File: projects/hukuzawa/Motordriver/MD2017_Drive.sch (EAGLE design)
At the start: 3 parts

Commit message: ドライバ駆動部回路図製作経過
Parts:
- added U$4: BUK116-50L, BUK116-50L:BUK116-50L
- added U$5, U$6: RELAY(L), relay:RELAY(L)
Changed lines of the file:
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@@
 <part name="U$2" library="FH105" deviceset="8PIN" device=""/>
 <part name="U$3" library="FH105" deviceset="8PIN" device=""/>
+<part name="U$4" library="BUK116-50L" deviceset="BUK116-50L" device=""/>
+<part name="U$5" library="relay" deviceset="RELAY(L)" device=""/>
+<part name="U$6" library="relay" deviceset="RELAY(L)" device=""/>
 </parts>
 <sheets>
@@
 <instance part="U$3" gate="-7" x="83.82" y="-25.4"/>
 <instance part="U$3" gate="-1" x="83.82" y="5.08"/>
+<instance part="U$4" gate="G$1" x="-22.86" y="35.56"/>
+<instance part="U$5" gate="R1" x="-68.58" y="5.08" rot="R180"/>
+<instance part="U$5" gate="1" x="-48.26" y="10.16" rot="R180"/>
+<instance part="U$5" gate="R2" x="-68.58" y="25.4" rot="R180"/>
+<instance part="U$6" gate="R1" x="-68.58" y="-35.56" rot="R180"/>
+<instance part="U$6" gate="1" x="-48.26" y="-30.48" rot="R180"/>
+<instance part="U$6" gate="R2" x="-68.58" y="-17.78" rot="R180"/>
 </instances>
 <busses>

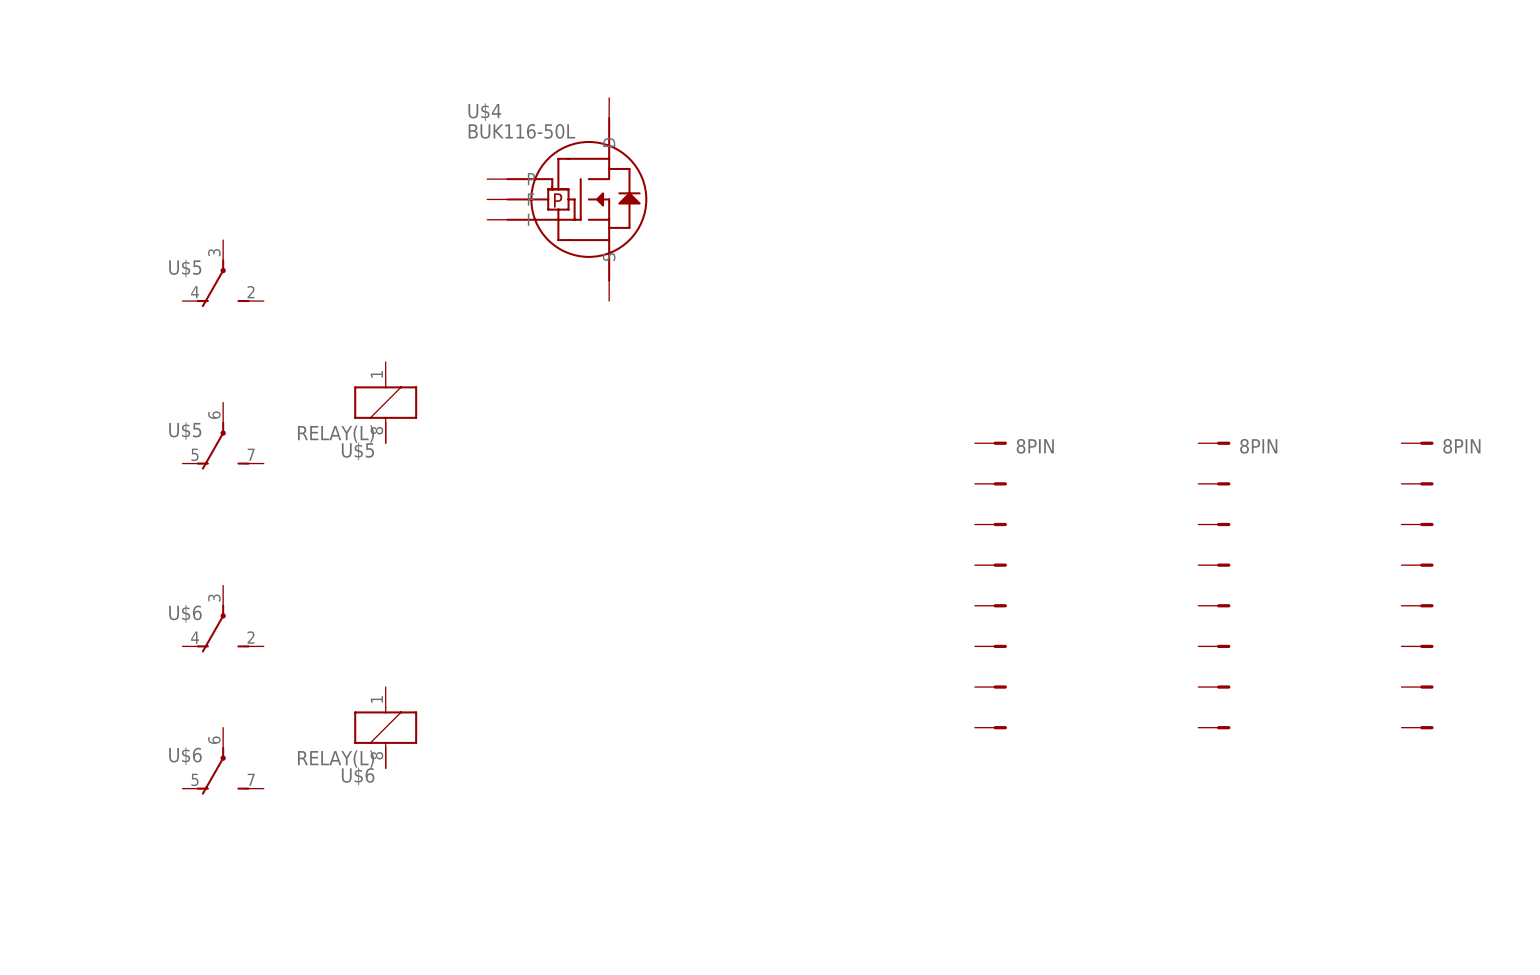
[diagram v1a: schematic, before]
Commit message: モータードライバ駆動部回路図製作途中
フォトカプラ追加、配線一部完了
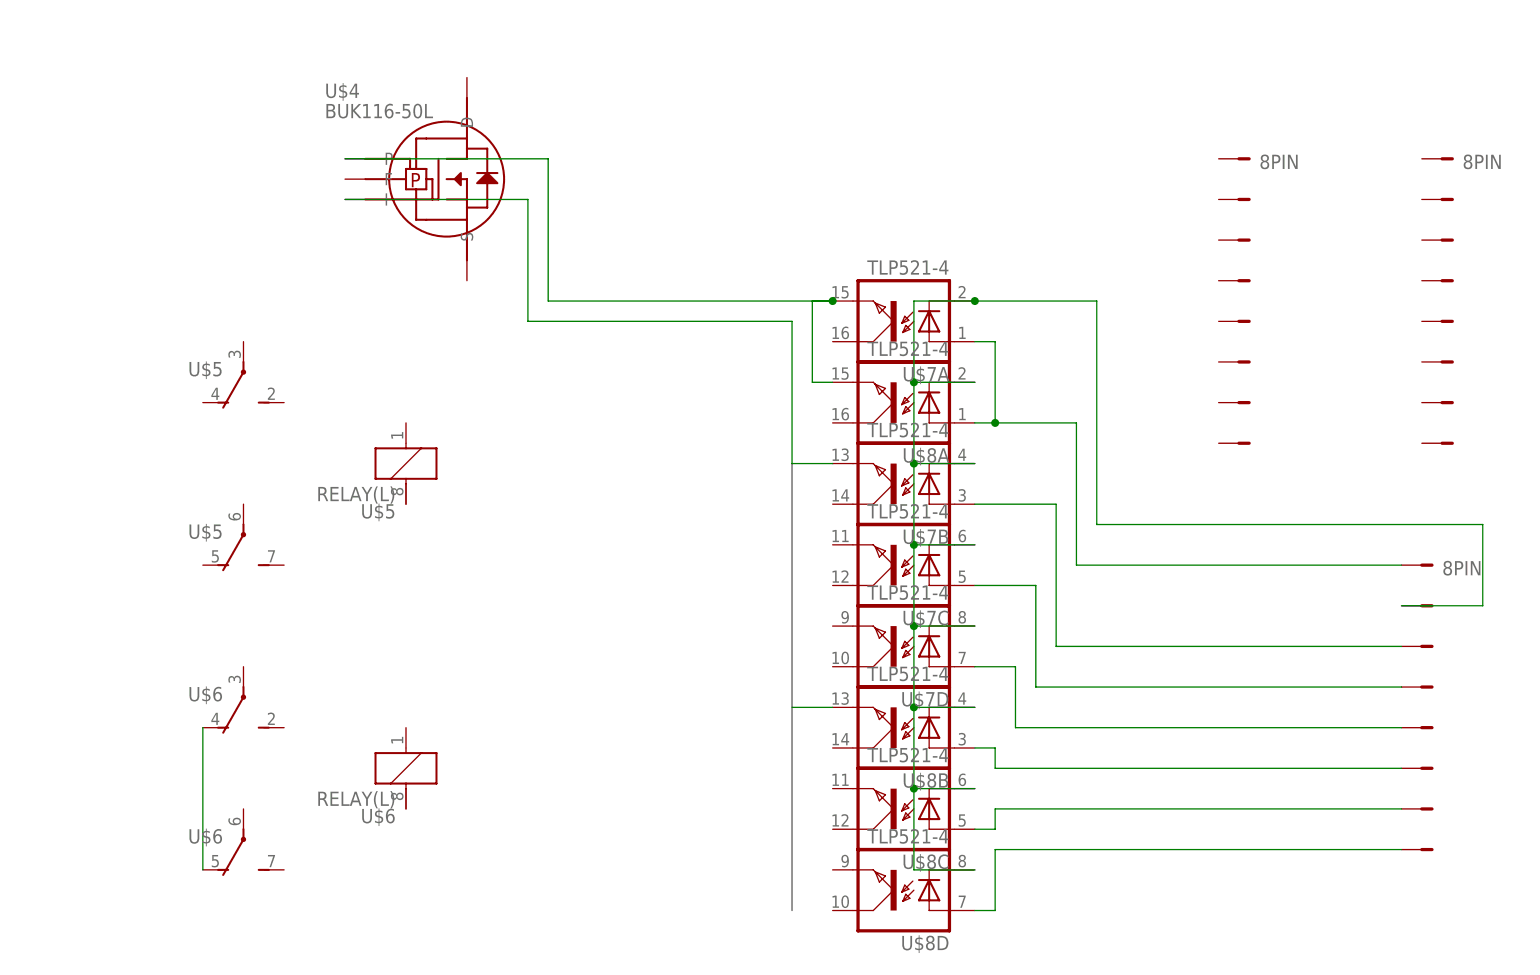
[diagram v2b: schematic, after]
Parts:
- added U$7, U$8: TLP521-4, photocoupler:TLP521-4
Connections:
- new net N$1: U$6R1.O, U$6R2.O
- new net N$10: U$4.P, U$7A.EMIT, U$8A.EMIT
- new net N$2: U$1-1.P$1, U$7A.A, U$8A.A
- new net N$3: U$1-2.P$1, U$7A.C, U$7B.C, U$7C.C, U$7D.C, U$8A.C, U$8B.C, U$8C.C, U$8D.C
- new net N$4: U$1-6.P$1, U$8B.A
- new net N$5: U$1-3.P$1, U$7B.A
- new net N$6: U$1-4.P$1, U$7C.A
- new net N$7: U$1-5.P$1, U$7D.A
- new net N$8: U$1-7.P$1, U$8C.A
- new net N$9: U$1-8.P$1, U$8D.A
- new net PWM: U$4.I, U$7B.EMIT, U$8B.EMIT
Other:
- moved on the sheet: U$4, U$5, U$6

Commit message: モータードライバ駆動部製作途中
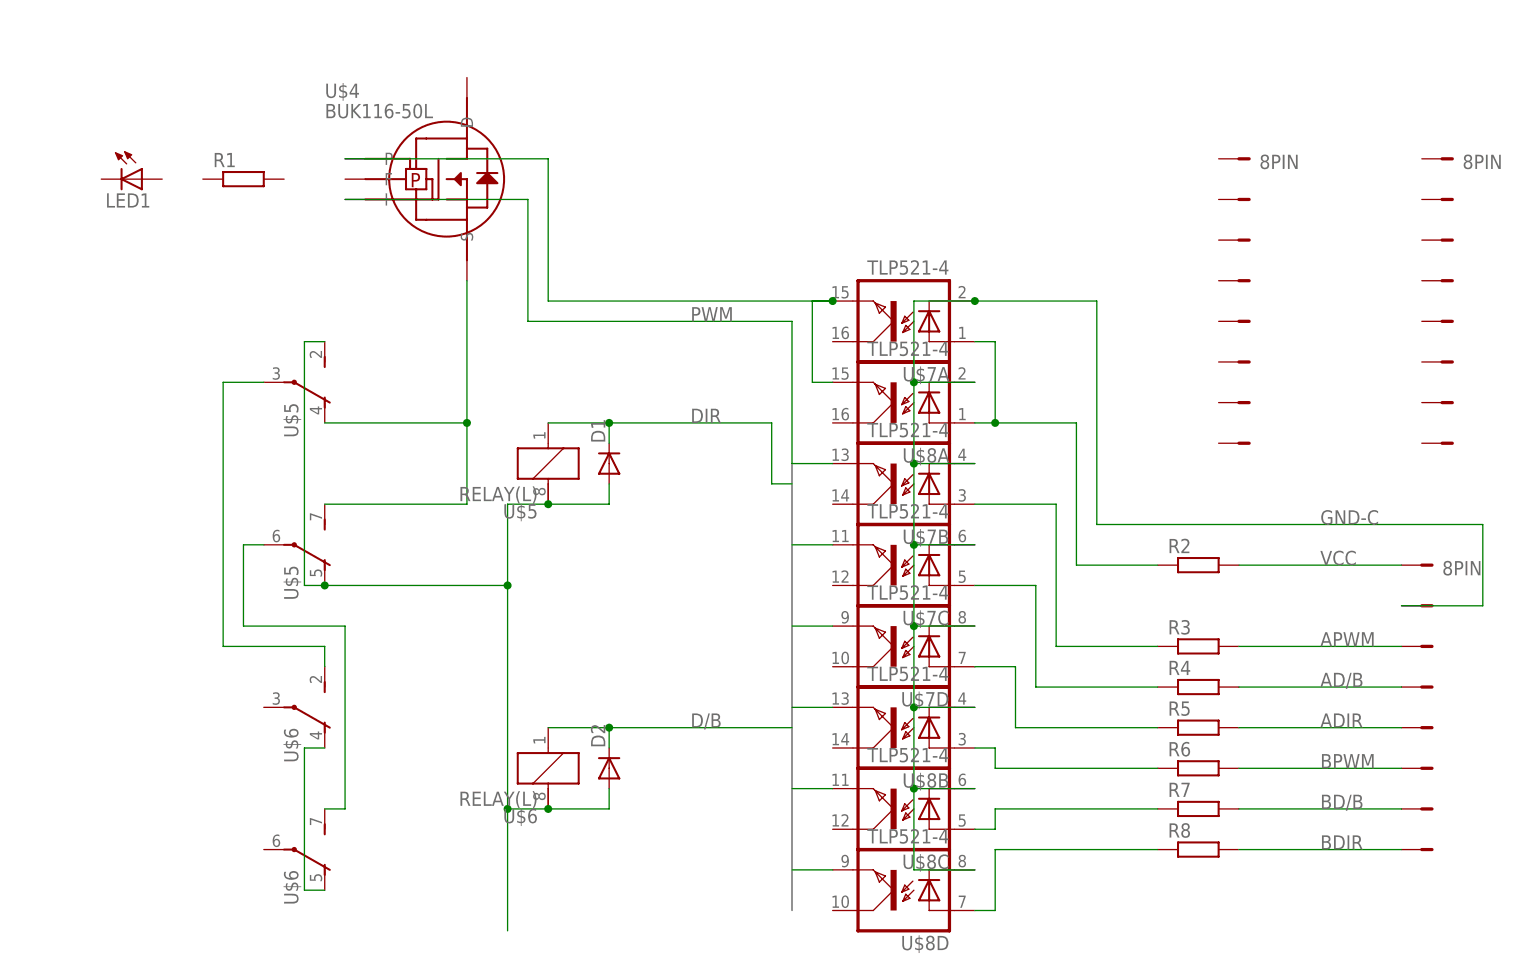
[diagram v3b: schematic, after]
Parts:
- added D1, D2: (no value), diode:DIODE7.5
- added LED1: (no value), FP-21T for MITS:LED5MM
- added R1, R2, R3, R4, R5, R6, R7, R8: (no value), rcl:R-EU_R3216W
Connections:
- net N$3 renamed GND-C
- removed net N$5: U$1-3.P$1, U$7B.A
- removed net N$6: U$1-4.P$1, U$7C.A
- removed net N$7: U$1-5.P$1, U$7D.A
- removed net N$8: U$1-7.P$1, U$8C.A
- removed net N$9: U$1-8.P$1, U$8D.A
- new net 2: R8.1, U$8D.A
- new net 3: R7.1, U$8C.A
- new net 4: R6.1, U$8B.A
- new net 5: R5.1, U$7D.A
- new net 6: R4.1, U$7C.A
- new net 7: R3.1, U$7B.A
- new net 8: R2.1, U$7A.A, U$8A.A
- new net AD/B: R4.2, U$1-4.P$1
- new net ADIR: R5.2, U$1-5.P$1
- new net APWM: R3.2, U$1-3.P$1
- new net BD/B: R7.2, U$1-7.P$1
- new net BDIR: R8.2, U$1-8.P$1
- new net BPWM: R6.2, U$1-6.P$1
- new net D/B: D2.C, U$61.1, U$7C.EMIT, U$8C.EMIT
- new net DIR: D1.C, U$51.1, U$7D.EMIT, U$8D.EMIT
- new net GND-D: D1.A, D2.A, U$51.2, U$5R1.O, U$5R2.S, U$61.2
- new net N$3: U$5R2.P, U$6R2.S
- new net VCC: R2.2, U$1-1.P$1
- net N$2: now also U$4.S, U$5R1.S, U$5R2.O; no longer U$1-1.P$1, U$7A.A, U$8A.A
- net N$4: now also U$5R1.P, U$6R1.S; no longer U$1-6.P$1, U$8B.A
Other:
- moved on the sheet: U$5, U$6

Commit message: モータードライバ駆動部回路図完成
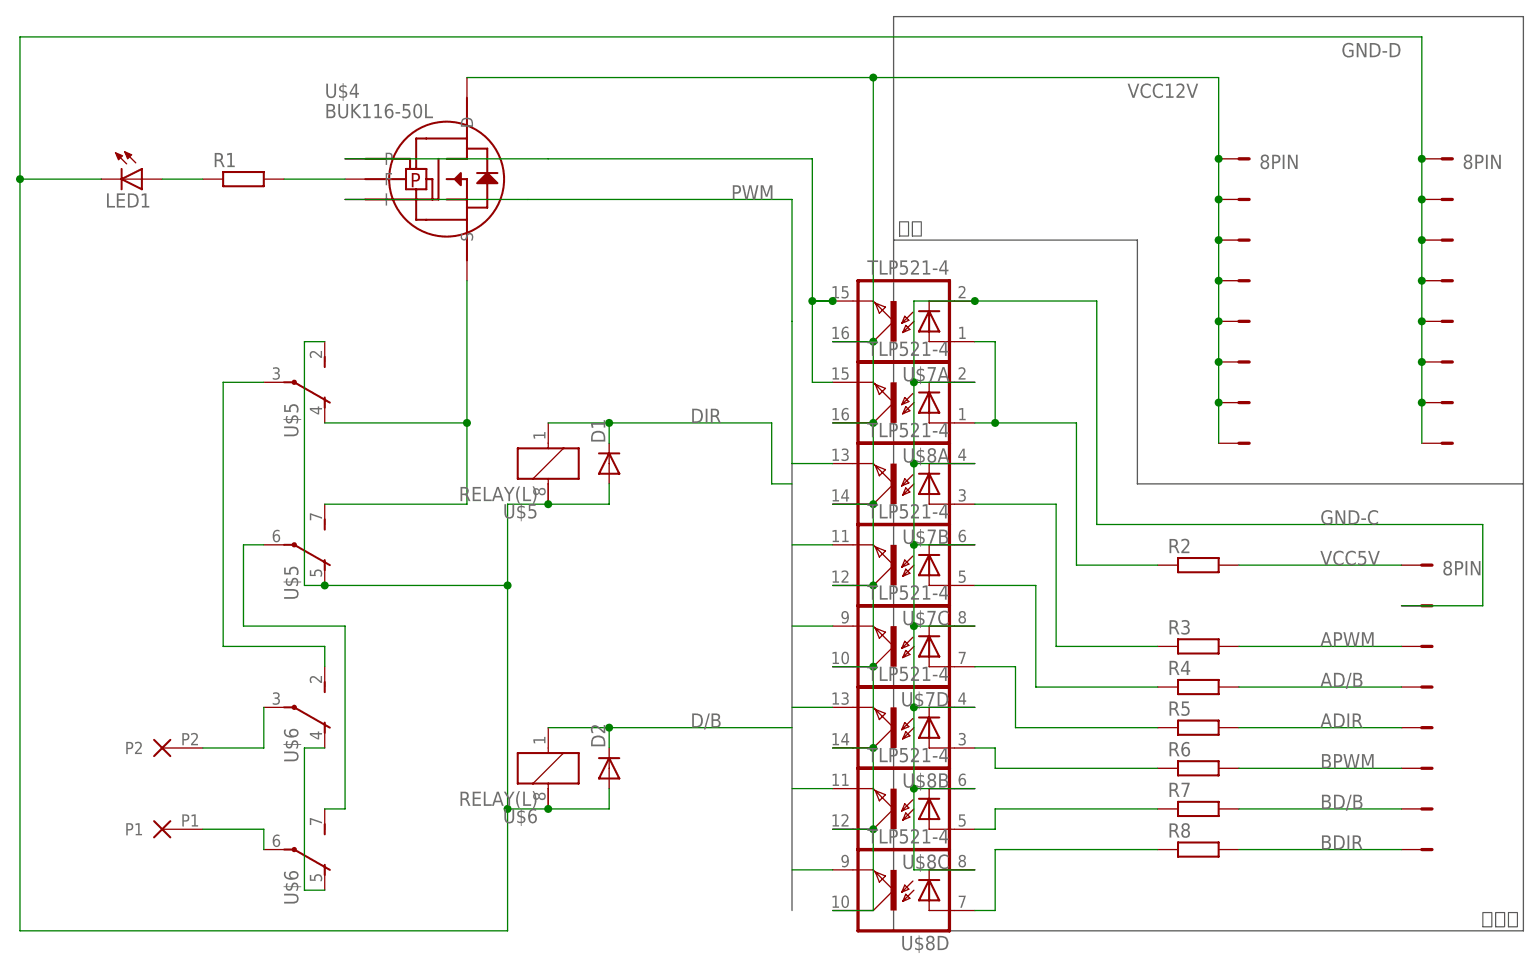
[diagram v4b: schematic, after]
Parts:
- added U$9: 2P, Powerio:2P
- renumbered U$1 to SIGNALPORT, U$2 to POWERPPORT, U$3 to POWERNPORT
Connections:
- net VCC renamed VCC5V
- new net N$5: U$6R1.P, U$9.P1
- new net N$6: U$6R2.P, U$9.P2
- new net N$7: R1.2, U$4.F
- new net N$8: LED1.A, R1.1
- new net VCC12V: POWERPPORT-1.P$1, POWERPPORT-2.P$1, POWERPPORT-3.P$1, POWERPPORT-4.P$1, POWERPPORT-5.P$1, POWERPPORT-6.P$1, POWERPPORT-7.P$1, POWERPPORT-8.P$1, U$4.D, U$7A.COL, U$7B.COL, U$7C.COL, U$7D.COL, U$8A.COL, U$8B.COL, U$8C.COL, U$8D.COL
- net GND-D: now also LED1.C, POWERNPORT-1.P$1, POWERNPORT-2.P$1, POWERNPORT-3.P$1, POWERNPORT-4.P$1, POWERNPORT-5.P$1, POWERNPORT-6.P$1, POWERNPORT-7.P$1, POWERNPORT-8.P$1
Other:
- note added: "制御部"
- note added: "電源"

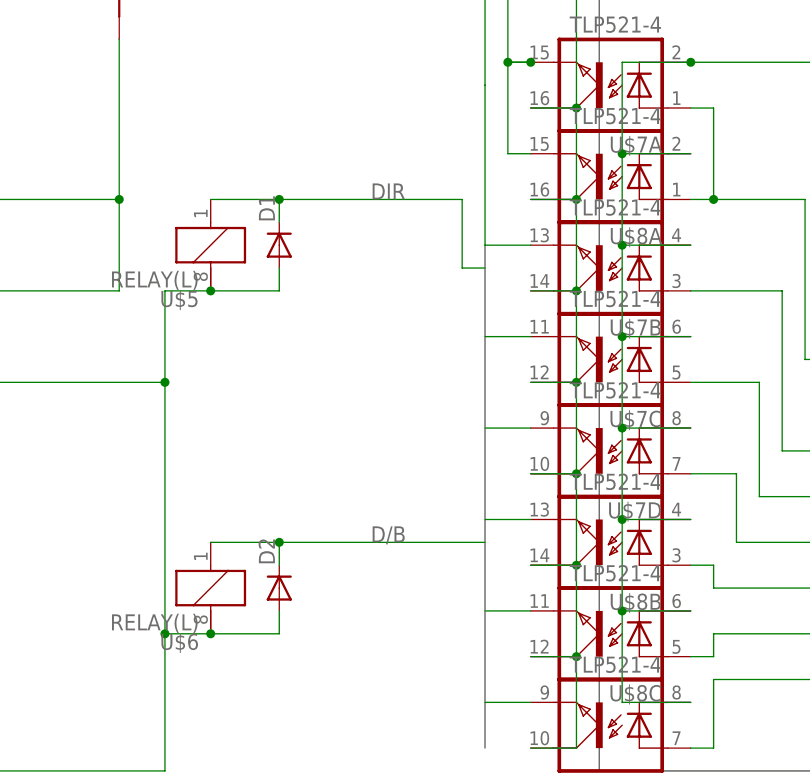
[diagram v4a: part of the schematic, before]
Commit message: モータードライバ駆動部修正
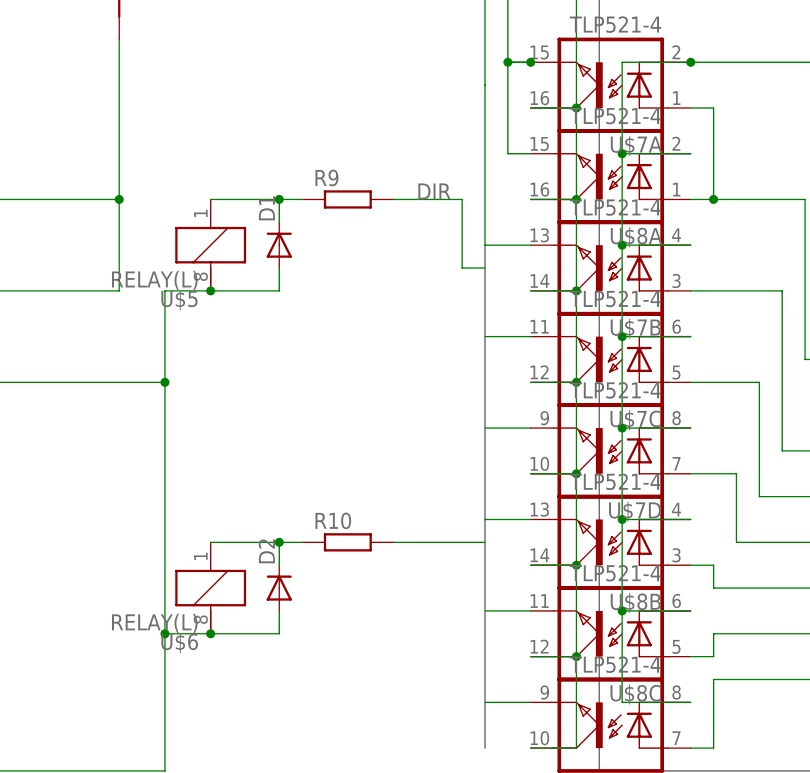
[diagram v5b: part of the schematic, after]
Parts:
- added R10, R9: (no value), rcl:R-EU_R3216W
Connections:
- new net 11: D2.C, R10.1, U$61.1
- new net N$9: D1.C, R9.1, U$51.1
- net D/B: now also R10.2; no longer D2.C, U$61.1
- net DIR: now also R9.2; no longer D1.C, U$51.1
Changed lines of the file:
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@@
 <part name="R8" library="rcl" deviceset="R-EU_" device="R3216W"/>
 <part name="U$9" library="Powerio" deviceset="2P" device=""/>
+<part name="R9" library="rcl" deviceset="R-EU_" device="R3216W"/>
+<part name="R10" library="rcl" deviceset="R-EU_" device="R3216W"/>
 </parts>
 <sheets>
@@
 <instance part="R8" gate="G$1" x="53.34" y="-45.72"/>
 <instance part="U$9" gate="G1" x="-76.2" y="-38.1" rot="R90"/>
+<instance part="R9" gate="G$1" x="-12.7" y="7.62"/>
+<instance part="R10" gate="G$1" x="-12.7" y="-30.48"/>
 </instances>
 <busses>
@@
 </segment>
 </net>
-<net name="D/B" class="0">
-<segment>
-<pinref part="U$7" gate="C" pin="EMIT"/>
-<wire x1="2.54" y1="-7.62" x2="7.62" y2="-7.62" width="0.1524" layer="91"/>
-</segment>
-<segment>
-<pinref part="U$8" gate="C" pin="EMIT"/>
-<wire x1="2.54" y1="-38.1" x2="7.62" y2="-38.1" width="0.1524" layer="91"/>
-</segment>
-<segment>
-<pinref part="U$6" gate="1" pin="1"/>
-<wire x1="2.54" y1="-30.48" x2="-20.32" y2="-30.48" width="0.1524" layer="91"/>
-<pinref part="D2" gate="G$1" pin="C"/>
-<wire x1="-20.32" y1="-30.48" x2="-27.94" y2="-30.48" width="0.1524" layer="91"/>
-<wire x1="-20.32" y1="-33.02" x2="-20.32" y2="-30.48" width="0.1524" layer="91"/>
-<junction x="-20.32" y="-30.48"/>
-<label x="-10.16" y="-30.48" size="1.778" layer="95"/>
-</segment>
-</net>
 <net name="DIR" class="0">
 <segment>
@@
 <wire x1="2.54" y1="0" x2="0" y2="0" width="0.1524" layer="91"/>
 <wire x1="0" y1="0" x2="0" y2="7.62" width="0.1524" layer="91"/>
-<pinref part="U$5" gate="1" pin="1"/>
-<wire x1="0" y1="7.62" x2="-20.32" y2="7.62" width="0.1524" layer="91"/>
-<pinref part="D1" gate="G$1" pin="C"/>
-<wire x1="-20.32" y1="7.62" x2="-27.94" y2="7.62" width="0.1524" layer="91"/>
-<wire x1="-20.32" y1="5.08" x2="-20.32" y2="7.62" width="0.1524" layer="91"/>
-<junction x="-20.32" y="7.62"/>
-<label x="-10.16" y="7.62" size="1.778" layer="95"/>
+<wire x1="0" y1="7.62" x2="-7.62" y2="7.62" width="0.1524" layer="91"/>
+<label x="-5.08" y="7.62" size="1.778" layer="95"/>
+<pinref part="R9" gate="G$1" pin="2"/>
 </segment>
 </net>
@@
 </segment>
 </net>
+<net name="N$9" class="0">
+<segment>
+<pinref part="U$5" gate="1" pin="1"/>
+<wire x1="-20.32" y1="7.62" x2="-27.94" y2="7.62" width="0.1524" layer="91"/>
+<pinref part="D1" gate="G$1" pin="C"/>
+<wire x1="-20.32" y1="5.08" x2="-20.32" y2="7.62" width="0.1524" layer="91"/>
+<junction x="-20.32" y="7.62"/>
+<wire x1="-17.78" y1="7.62" x2="-20.32" y2="7.62" width="0.1524" layer="91"/>
+<pinref part="R9" gate="G$1" pin="1"/>
+</segment>
+</net>
+<net name="11" class="0">
+<segment>
+<pinref part="U$6" gate="1" pin="1"/>
+<pinref part="D2" gate="G$1" pin="C"/>
+<wire x1="-20.32" y1="-30.48" x2="-27.94" y2="-30.48" width="0.1524" layer="91"/>
+<wire x1="-20.32" y1="-33.02" x2="-20.32" y2="-30.48" width="0.1524" layer="91"/>
+<pinref part="R10" gate="G$1" pin="1"/>
+<wire x1="-17.78" y1="-30.48" x2="-20.32" y2="-30.48" width="0.1524" layer="91"/>
+<junction x="-20.32" y="-30.48"/>
+</segment>
+</net>
+<net name="D/B" class="0">
+<segment>
+<pinref part="R10" gate="G$1" pin="2"/>
+<wire x1="-7.62" y1="-30.48" x2="2.54" y2="-30.48" width="0.1524" layer="91"/>
+</segment>
+<segment>
+<pinref part="U$7" gate="C" pin="EMIT"/>
+<wire x1="7.62" y1="-7.62" x2="2.54" y2="-7.62" width="0.1524" layer="91"/>
+</segment>
+<segment>
+<pinref part="U$8" gate="C" pin="EMIT"/>
+<wire x1="7.62" y1="-38.1" x2="2.54" y2="-38.1" width="0.1524" layer="91"/>
+</segment>
+</net>
